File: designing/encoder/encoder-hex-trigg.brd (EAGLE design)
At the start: 17.8 x 27.6 mm, 17 parts, among them SW1 EC12E_SW, U1 SN74LVC1G14DBVRDBV5-L, U2 SN74LVC1G14DBVRDBV5-L, U3 SN74LVC1G14DBVRDBV5-L

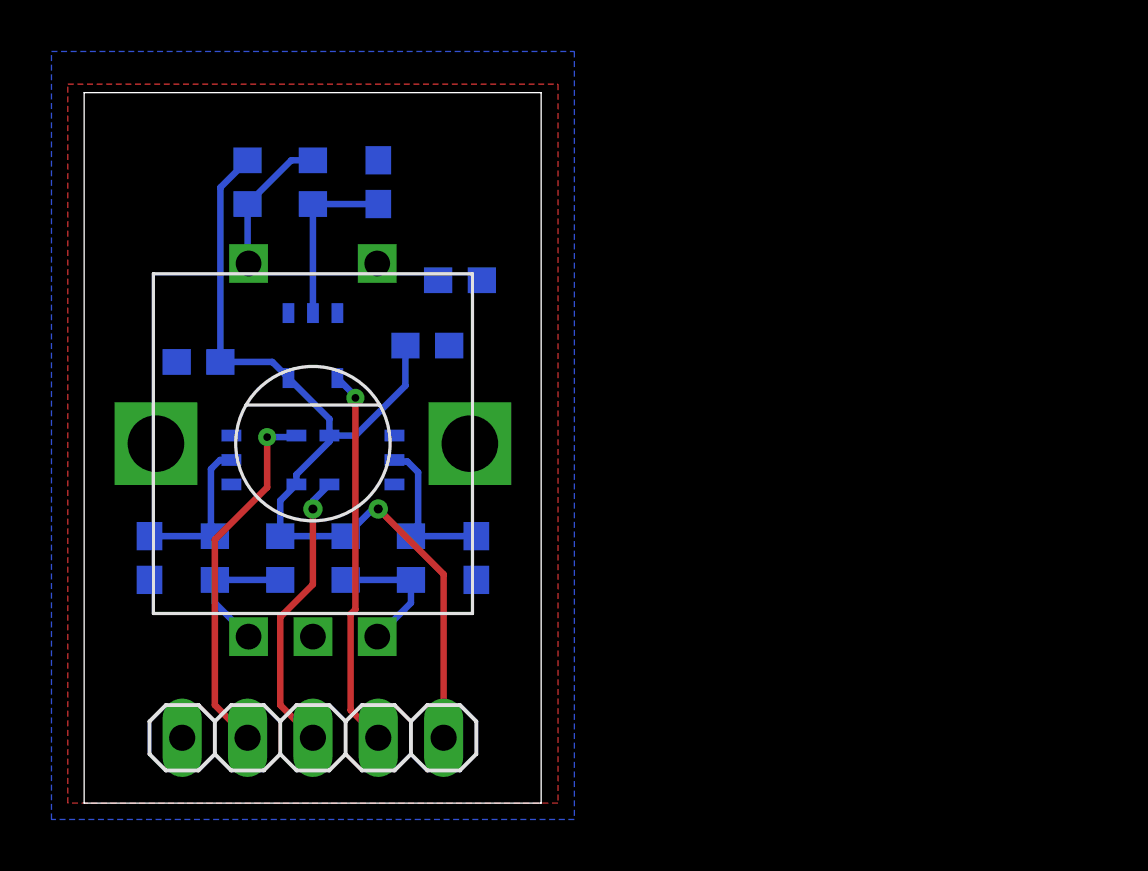
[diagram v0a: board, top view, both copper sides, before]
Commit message: Added dual encoder module
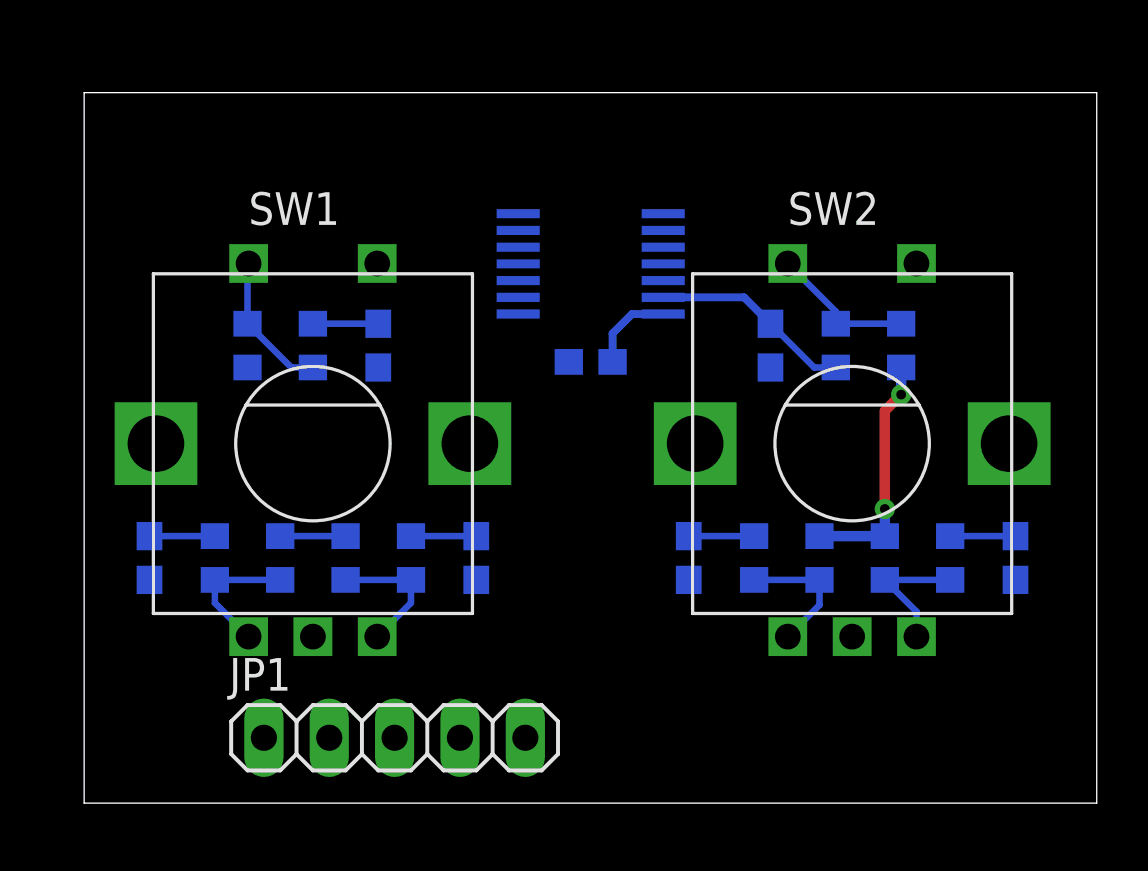
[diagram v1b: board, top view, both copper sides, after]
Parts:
- removed U1, U3: SN74LVC1G14DBVRDBV5-L, 0000-master:DBV5-L
- added C7: 10n, rcl:C0603
- added R10, R11, R12, R7, R8, R9: 10k, rcl:R0603
- added SW2: EC12E_SW, switch-alps:ALPS_EC12E_SW
- C5, C6: value 100n -> 10n
- U2: value SN74LVC1G14DBVRDBV5-L -> SN74HC14QPWRQ1; device 0000-master:DBV5-L -> SparkFun-PowerSymbols:PW14
- moved C6 24.1 mm to (36.2, 9.53), turned to 270 degrees
- moved C5 22.2 mm to (26.7, 17.8), turned to 90 degrees
- moved U2 14.8 mm to (19.7, 21.0)
- moved C4 6.38 mm to (19.7, 17.1), turned to 0 degrees
- moved C1 6.35 mm to (11.4, 17.8), turned to 90 degrees
- moved R1 6.35 mm to (8.89, 17.8), turned to 90 degrees
- moved R2 6.35 mm to (6.35, 17.8), turned to 270 degrees
- moved JP1 3.17 mm to (12.1, 2.54)
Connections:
- removed net A: JP1.2, U2.4
- removed net A_RC: C3.1, R4.1, U2.2
- removed net B: JP1.3, U3.4
- removed net B_RC: C2.1, R3.1, U3.2
- removed net SW: JP1.4, U1.4
- removed net SW_RC: C1.2, R1.2, U1.2
- new net A1: JP1.2, U2.2
- new net A1_RC: C3.1, R4.1, U2.1
- new net A2: U2.8
- new net A2_RC: C7.1, R10.1, U2.9
- new net B1: JP1.3, U2.4
- new net B1_RC: C2.1, R3.1, U2.3
- new net B2: U2.10
- new net B2_RC: C6.1, R9.1, U2.11
- new net N$2: R7.1, R8.1, SW2.D
- new net N$5: R11.1, R9.2, SW2.B
- new net N$6: R10.2, R12.1, SW2.A
- new net SW1: JP1.4, U2.6
- new net SW1_RC: C1.2, R1.2, U2.5
- new net SW2: U2.12
- new net SW2_RC: C5.2, R7.2, U2.13
- net 3.3V: now also R11.2, R12.2, R8.2, U2.14; no longer C5.1, C6.1, U1.5, U2.5, U3.5
- net PE: now also C5.1, C7.2, SW2.C, SW2.E, U2.7; no longer C5.2, U1.1, U1.3, U2.1, U2.3, U3.1, U3.3
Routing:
- net 3.3V: track 38.3 -> 15.5 mm, vias 1 -> 2
- net SW: track 14.8 -> 0.00 mm, vias 1 -> 0
- net A: track 14.2 -> 0.00 mm, vias 1 -> 0
- net B: track 11.2 -> 0.00 mm, vias 1 -> 0
- net SW2_RC: track 0.00 -> 7.83 mm
- net SW_RC: track 6.78 -> 0.00 mm
- net B_RC: track 6.26 -> 0.00 mm
- net A_RC: track 6.15 -> 0.00 mm
- net N$2: track 0.00 -> 5.65 mm
- net N$5: track 0.00 -> 5.25 mm
- net N$6: track 0.00 -> 5.25 mm
- net B1_RC: track 0.00 -> 2.94 mm
- net A1_RC: track 0.00 -> 2.54 mm
- net SW1_RC: track 0.00 -> 2.54 mm
- net B2_RC: track 0.00 -> 2.54 mm
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- removed copper zone on layer 1, net PE
- removed copper zone on layer 16, net PE
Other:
- board size 17.8 x 27.6 mm -> 39.4 x 27.6 mm
